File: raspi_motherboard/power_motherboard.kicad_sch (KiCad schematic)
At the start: 19 parts, among them J1 GPIO, J2 Conn_02x04_Top_Bottom

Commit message: small fixes
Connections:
- no-connect marks 0 -> 14

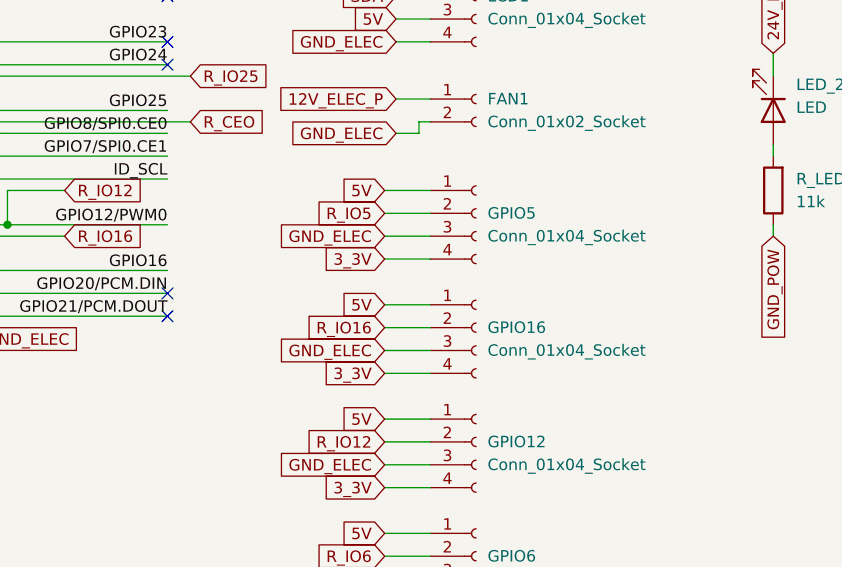
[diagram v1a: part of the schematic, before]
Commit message: add Tirette&Buttons connector (not routed yet, as the CAN schematic is broken)
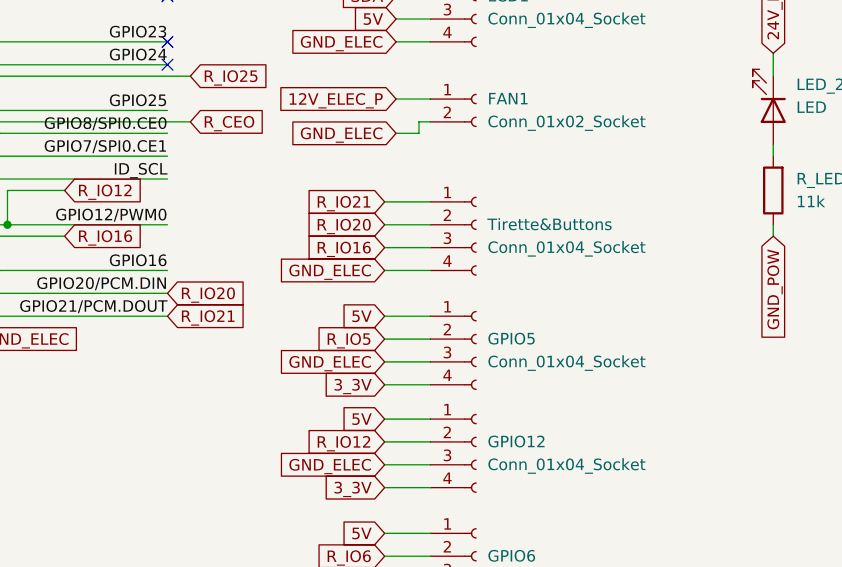
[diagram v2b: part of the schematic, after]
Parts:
- renumbered GPIO16 to Tirette&Buttons
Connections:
- net +3V3: no longer Tirette&Buttons.4 (Pin_4)
- net +5V: no longer Tirette&Buttons.1 (Pin_1)
- net GND: now also Tirette&Buttons.4 (Pin_4); no longer Tirette&Buttons.3 (Pin_3)
- net R_IO16: now also Tirette&Buttons.3 (Pin_3); no longer Tirette&Buttons.2 (Pin_2)
- net GPIO20/PCM.DIN renamed R_IO20
- net R_IO20: now also Tirette&Buttons.2 (Pin_2)
- net GPIO21/PCM.DOUT renamed R_IO21
- net R_IO21: now also Tirette&Buttons.1 (Pin_1)
- no-connect marks 14 -> 12
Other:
- moved on the sheet: GPIO5, Tirette&Buttons

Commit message: Commit missed element
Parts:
- renumbered Tirette&Buttons to Tirette&Buttons1
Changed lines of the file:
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@@
 	(label "ID_SDA"
 		(at 31.75 60.96 0)
-		(fields_autoplaced yes)
 		(effects
 			(font
@@
 	(label "GPIO6"
 		(at 31.75 66.04 0)
-		(fields_autoplaced yes)
 		(effects
 			(font
@@
 	(label "ID_SCL"
 		(at 100.33 60.96 180)
-		(fields_autoplaced yes)
 		(effects
 			(font
@@
 	(label "GPIO5"
 		(at 31.75 63.5 0)
-		(fields_autoplaced yes)
 		(effects
 			(font
@@
 	(label "GPIO21{slash}PCM.DOUT"
 		(at 100.33 76.2 180)
-		(fields_autoplaced yes)
 		(effects
 			(font
@@
 	(label "GPIO19{slash}PCM.FS"
 		(at 31.75 71.12 0)
-		(fields_autoplaced yes)
 		(effects
 			(font
@@
 	(label "GPIO10{slash}SPI0.MOSI"
 		(at 31.75 50.8 0)
-		(fields_autoplaced yes)
 		(effects
 			(font
@@
 	(label "GPIO9{slash}SPI0.MISO"
 		(at 31.75 53.34 0)
-		(fields_autoplaced yes)
 		(effects
 			(font
@@
 	(label "GPIO23"
 		(at 100.33 45.72 180)
-		(fields_autoplaced yes)
 		(effects
 			(font
@@
 	(label "GPIO4{slash}GPCLK0"
 		(at 31.75 35.56 0)
-		(fields_autoplaced yes)
 		(effects
 			(font
@@
 	(label "GPIO27"
 		(at 31.75 43.18 0)
-		(fields_autoplaced yes)
 		(effects
 			(font
@@
 	(label "GPIO26"
 		(at 31.75 73.66 0)
-		(fields_autoplaced yes)
 		(effects
 			(font
@@
 	(label "GPIO14{slash}TXD0"
 		(at 100.33 35.56 180)
-		(fields_autoplaced yes)
 		(effects
 			(font
@@
 	(label "GPIO8{slash}SPI0.CE0"
 		(at 100.33 55.88 180)
-		(fields_autoplaced yes)
 		(effects
 			(font
@@
 	(label "GPIO15{slash}RXD0"
 		(at 100.33 38.1 180)
-		(fields_autoplaced yes)
 		(effects
 			(font
@@
 	(label "GPIO16"
 		(at 100.33 71.12 180)
-		(fields_autoplaced yes)
 		(effects
 			(font
@@
 	(label "GPIO22"
 		(at 31.75 45.72 0)
-		(fields_autoplaced yes)
 		(effects
 			(font
@@
 	(label "GPIO2{slash}SDA1"
 		(at 31.75 30.48 0)
-		(fields_autoplaced yes)
 		(effects
 			(font
@@
 	(label "GPIO17"
 		(at 31.75 40.64 0)
-		(fields_autoplaced yes)
 		(effects
 			(font
@@
 	(label "GPIO25"
 		(at 100.33 53.34 180)
-		(fields_autoplaced yes)
 		(effects
 			(font
@@
 	(label "GPIO3{slash}SCL1"
 		(at 31.75 33.02 0)
-		(fields_autoplaced yes)
 		(effects
 			(font
@@
 	(label "GPIO18{slash}PCM.CLK"
 		(at 100.33 40.64 180)
-		(fields_autoplaced yes)
 		(effects
 			(font
@@
 	(label "GPIO12{slash}PWM0"
 		(at 100.33 66.04 180)
-		(fields_autoplaced yes)
 		(effects
 			(font
@@
 	(label "GPIO13{slash}PWM1"
 		(at 31.75 68.58 0)
-		(fields_autoplaced yes)
 		(effects
 			(font
@@
 	(label "GPIO20{slash}PCM.DIN"
 		(at 100.33 73.66 180)
-		(fields_autoplaced yes)
 		(effects
 			(font
@@
 	(label "GPIO24"
 		(at 100.33 48.26 180)
-		(fields_autoplaced yes)
 		(effects
 			(font
@@
 	(label "GPIO7{slash}SPI0.CE1"
 		(at 100.33 58.42 180)
-		(fields_autoplaced yes)
 		(effects
 			(font
@@
 	(label "GPIO11{slash}SPI0.SCLK"
 		(at 31.75 55.88 0)
-		(fields_autoplaced yes)
 		(effects
 			(font
@@
 		(dnp no)
 		(fields_autoplaced yes)
-		(property "Reference" "Tirette&Buttons"
+		(property "Reference" "Tirette&Buttons1"
 			(at 135.89 66.0399 0)
 			(effects
@@
 			(project "power_motherboard"
 				(path "/e63e39d7-6ac0-4ffd-8aa3-1841a4541b55"
-					(reference "Tirette&Buttons")
+					(reference "Tirette&Buttons1")
 					(unit 1)
 				)
